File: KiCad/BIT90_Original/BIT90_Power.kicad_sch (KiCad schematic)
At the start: 16 parts, among them Q7 2SA684, Q8 2N2222

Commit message: Added "Processor" Sheet 6-1
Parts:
- added U14: 74LS05, symbol 74xx:74LS05
- added U6: 74LS74, symbol 74xx:74LS74
- added U9: 74LS32, symbol 74xx:74LS32
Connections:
- net +5V: now also U14.14 (VCC), U6.14 (VCC), U9.14 (VCC)
- net GND: now also U14.7 (GND), U6.7 (GND), U9.7 (GND)

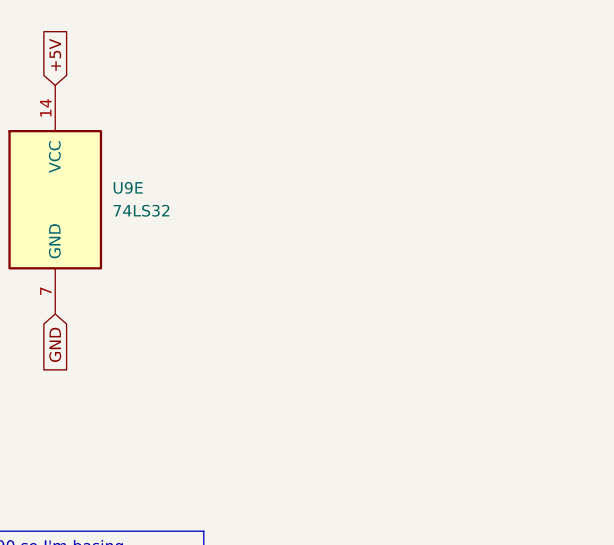
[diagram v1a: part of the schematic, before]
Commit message: Added "Video Control" schematic
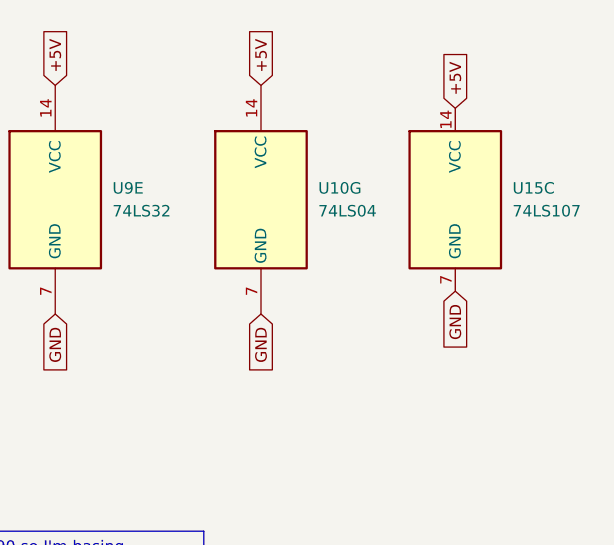
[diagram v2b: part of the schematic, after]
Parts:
- added U10: 74LS04, symbol 74xx:74LS04
- added U15: 74LS107, symbol 74xx:74LS107
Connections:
- net +5V: now also U10.14 (VCC), U15.14 (VCC)
- net GND: now also U10.7 (GND), U15.7 (GND)

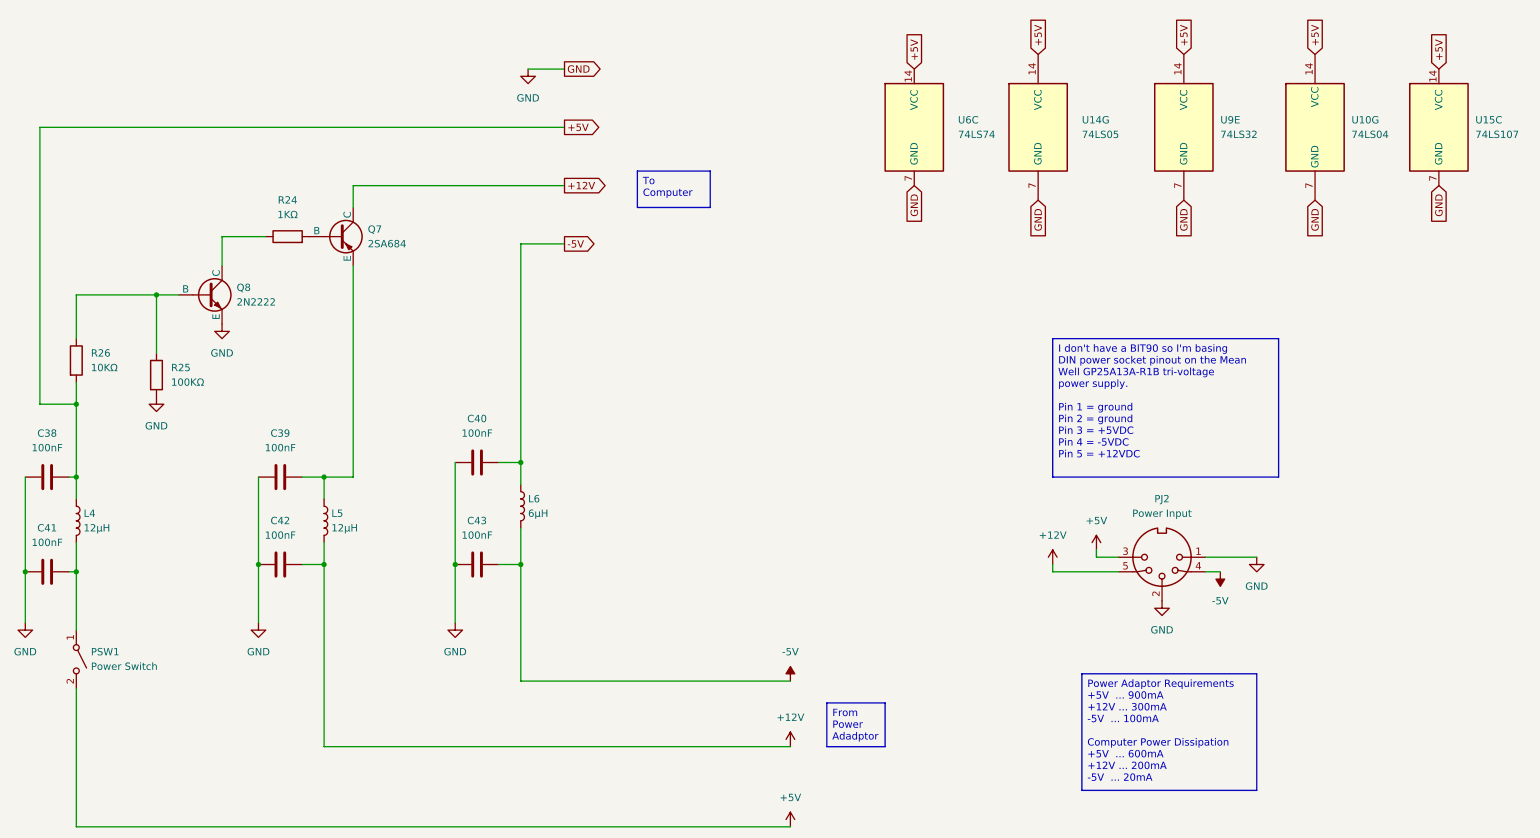
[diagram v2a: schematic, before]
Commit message: Added "Joystick, Audio, Tape Out" schematic
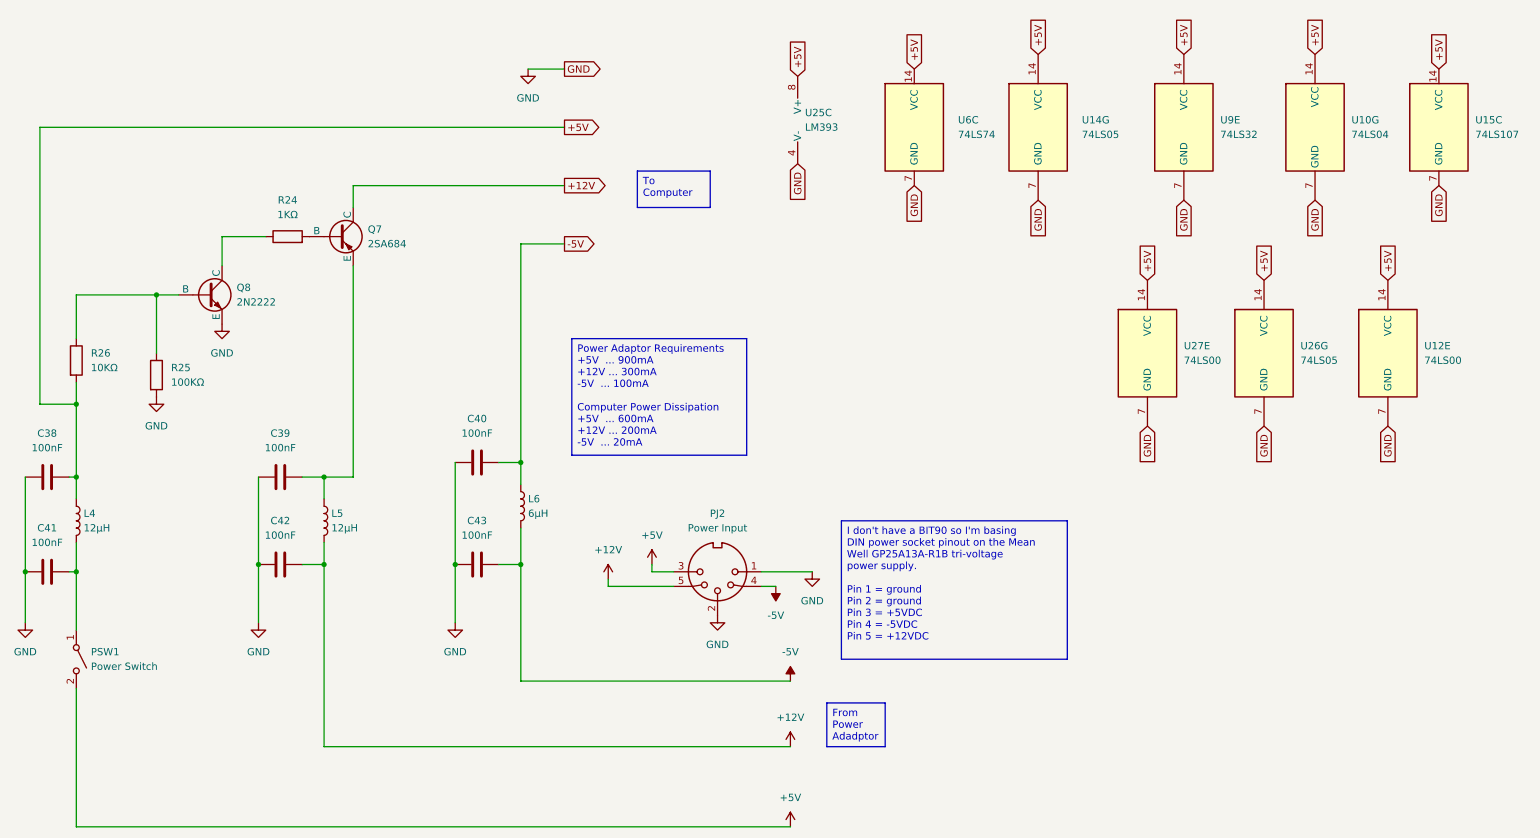
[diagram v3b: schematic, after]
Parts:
- added U12, U27: 74LS00, symbol 74xx:74LS00
- added U25: LM393, symbol Comparator:LM393
- added U26: 74LS05, symbol 74xx:74LS05
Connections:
- net +5V: now also U12.14 (VCC), U25.8 (V+), U26.14 (VCC), U27.14 (VCC)
- net GND: now also U12.7 (GND), U25.4 (V-), U26.7 (GND), U27.7 (GND)
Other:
- moved on the sheet: PJ2

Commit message: Completed original schematic redraw
Well, didn't finish the Video Encoder (PAL) sheet as I'm not going to use any of it in the new design.
Moved the audio output from that sheet to the Joystick/Audio/Tape out sheet where the sound generator is.
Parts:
- added U28: CD4066BE, Package_DIP:DIP-14_W7.62mm, symbol Analog_Switch:CD4066BE
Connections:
- net +12V: now also U28.14 (V_{DD})
- net GND: now also U28.7 (V_{SS})
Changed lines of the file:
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@@
 	(generator "eeschema")
 	(generator_version "9.0")
-	(paper "A4")
+	(paper "A3")
 	(title_block
 		(title "BIT90 Power")
 		(date "3/JUN/2026")
-		(rev "WIP")
+		(rev "A")
 		(company "Brett Hallen")
 		(comment 3 "From Sheet 6-4")
@@
 		)
 	)
+	(global_label "+12V"
+		(shape input)
+		(at 205.74 66.04 90)
+		(fields_autoplaced yes)
+		(effects
+			(font
+				(size 1.27 1.27)
+			)
+			(justify left)
+		)
+		(property "Intersheetrefs" "${INTERSHEET_REFS}"
+			(at 205.74 57.9748 90)
+			(effects
+				(font
+					(size 1.27 1.27)
+				)
+				(justify left)
+				(hide yes)
+			)
+		)
+	)
 	(global_label "GND"
 		(shape input)
@@
 				)
 				(justify left)
+				(hide yes)
+			)
+		)
+	)
+	(global_label "GND"
+		(shape input)
+		(at 205.74 81.28 270)
+		(fields_autoplaced yes)
+		(effects
+			(font
+				(size 1.27 1.27)
+			)
+			(justify right)
+		)
+		(property "Intersheetrefs" "${INTERSHEET_REFS}"
+			(at 205.74 88.1357 90)
+			(effects
+				(font
+					(size 1.27 1.27)
+				)
+				(justify right)
 				(hide yes)
 			)
@@
 				)
 			)
+		)
+	)
+	(symbol
+		(lib_id "Analog_Switch:CD4066BE")
+		(at 205.74 73.66 0)
+		(unit 5)
+		(exclude_from_sim no)
+		(in_bom yes)
+		(on_board yes)
+		(dnp no)
+		(fields_autoplaced yes)
+		(property "Reference" "U28"
+			(at 210.82 72.3899 0)
+			(effects
+				(font
+					(size 1.27 1.27)
+				)
+				(justify left)
+			)
+		)
+		(property "Value" "CD4066BE"
+			(at 210.82 74.9299 0)
+			(effects
+				(font
+					(size 1.27 1.27)
+				)
+				(justify left)
+			)
+		)
+		(property "Footprint" "Package_DIP:DIP-14_W7.62mm"
+			(at 205.74 76.2 0)
+			(effects
+				(font
+					(size 1.27 1.27)
+				)
+				(hide yes)
+			)
+		)
+		(property "Datasheet" "https://www.ti.com/lit/ds/symlink/cd4066b.pdf"
+			(at 205.74 73.66 0)
+			(effects
+				(font
+					(size 1.27 1.27)
+				)
+				(hide yes)
+			)
+		)
+		(property "Description" "Quad 20V analog SPST 1:1 switch, DIP-14"
+			(at 205.74 73.66 0)
+			(effects
+				(font
+					(size 1.27 1.27)
+				)
+				(hide yes)
+			)
+		)
+		(pin "5"
+		)
+		(pin "4"
+		)
+		(pin "2"
+		)
+		(pin "13"
+		)
+		(pin "1"
+		)
+		(pin "6"
+		)
+		(pin "9"
+		)
+		(pin "11"
+		)
+		(pin "7"
+		)
+		(pin "14"
+		)
+		(pin "10"
+		)
+		(pin "12"
+		)
+		(pin "3"
+		)
+		(pin "8"
+		)
+		(instances
+			(project "BIT90_Original"
+				(path "/d65498c3-6385-4920-ac0f-4c76daf90780/f4c67384-cc43-4b93-aeab-fb15189bac5d"
+					(reference "U28")
+					(unit 5)
+				)
+			)
